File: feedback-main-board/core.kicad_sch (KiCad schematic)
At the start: 38 parts, among them SW1 SW_SPDT, SW2 SW_SPDT, U1 TL074, U2 TL074

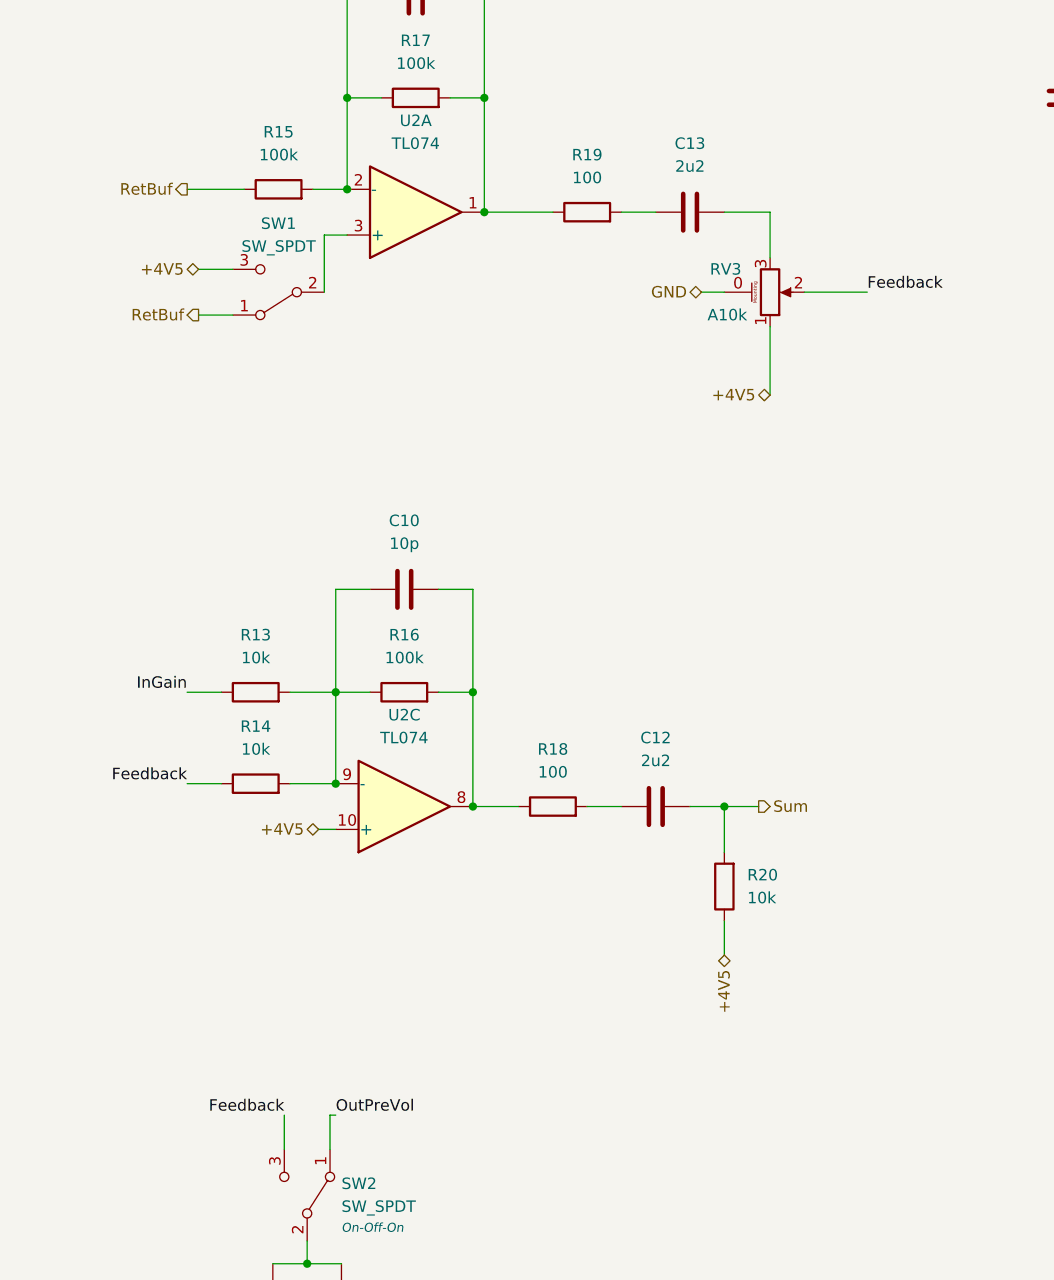
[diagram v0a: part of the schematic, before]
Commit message: Move clipping to pre-feedback
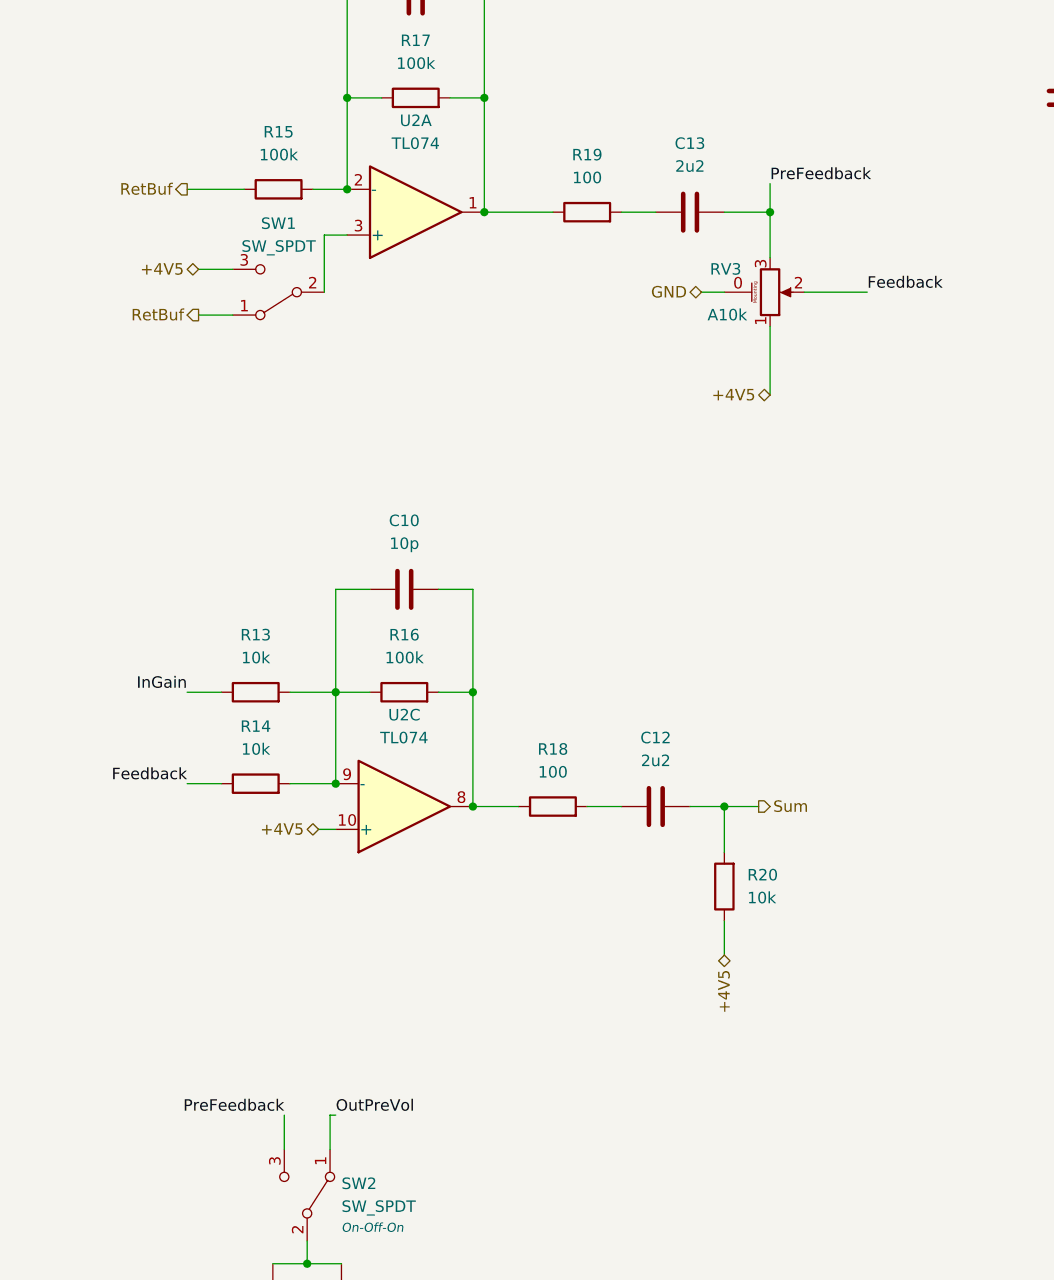
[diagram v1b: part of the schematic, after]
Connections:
- net Feedback: no longer SW2.3 (C)
- net PreFeedback: now reaches C13.2, RV3.3
- net PreFeedback: now also SW2.3 (C)
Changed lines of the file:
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@@
   (junction (at 253.365 45.72) (diameter 0) (color 0 0 0 0)
   )
+  (junction (at 207.01 48.26) (diameter 0) (color 0 0 0 0)
+  )
   (junction (at 93.98 171.45) (diameter 0) (color 0 0 0 0)
   )
@@
   )
   (wire (pts (xy 170.18 101.6) (xy 173.99 101.6))
+    (stroke (width 0) (type default) (color 0 0 0 0))
+  )
+  (wire (pts (xy 207.01 45.085) (xy 207.01 48.26))
     (stroke (width 0) (type default) (color 0 0 0 0))
   )
@@
     (effects (font (size 1 1) italic) (justify left bottom))
   )
-  (label "Feedback" (at 153.035 148.59 180)
+  (label "PreFeedback" (at 153.035 148.59 180)
     (effects (font (size 1.27 1.27)) (justify right bottom))
   )
@@
     (effects (font (size 1.27 1.27)) (justify left bottom))
   )
+  (label "PreFeedback" (at 207.01 45.085 0)
+    (effects (font (size 1.27 1.27)) (justify left bottom))
+  )

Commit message: Changes pre-rev3
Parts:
- C10, C11: LCSC (none) -> C1634
- C12, C13, C5, C6, C7, C8, C9, D2, D3, D4, D5, RV1, RV2, RV3, SW1, SW2: LCSC (none) -> DNP
- C14, C15: LCSC (none) -> C14663; Mouser (none) -> 581-06035C105MAT2A
- R10, R11, R18, R19, R9: LCSC (none) -> C22775
- R12, R13, R14, R20: LCSC (none) -> C25804
- R15, R16, R17, R6, R8: LCSC (none) -> C25803
- R5, R7: LCSC (none) -> C22935
- U1, U2: LCSC (none) -> C6964
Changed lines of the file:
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@@
   (title_block
     (title "Read/Repeat")
-    (date "2025-01-24")
-    (rev "v1rev1")
+    (date "2025-03-14")
+    (rev "v1rev3")
     (company "Pedal Markt / Andrei Salomatin")
   )
@@
     )
     (property "Mouser" "595-TL074IDR" (id 4) (at 167.64 48.26 0)
+      (effects (font (size 1.27 1.27)) hide)
+    )
+    (property "LCSC" "C6964" (id 5) (at 167.64 48.26 0)
       (effects (font (size 1.27 1.27)) hide)
     )
@@
       (effects (font (size 1.27 1.27)) hide)
     )
+    (property "LCSC" "DNP" (id 5) (at 35.56 116.84 0)
+      (effects (font (size 1.27 1.27)) hide)
+    )
     (pin "1")
     (pin "2")
@@
     )
     (property "Datasheet" "~" (id 3) (at 167.64 24.13 0)
+      (effects (font (size 1.27 1.27)) hide)
+    )
+    (property "LCSC" "C1634" (id 4) (at 167.64 24.13 0)
       (effects (font (size 1.27 1.27)) hide)
     )
@@
       (effects (font (size 1.27 1.27)) hide)
     )
+    (property "LCSC" "DNP" (id 4) (at 207.01 57.15 0)
+      (effects (font (size 1.27 1.27)) hide)
+    )
     (pin "0")
     (pin "1")
@@
       (effects (font (size 1.27 1.27)) hide)
     )
+    (property "LCSC" "C22775" (id 4) (at 73.66 48.26 0)
+      (effects (font (size 1.27 1.27)) hide)
+    )
     (pin "1")
     (pin "2")
@@
       (effects (font (size 1.27 1.27)) hide)
     )
+    (property "LCSC" "DNP" (id 4) (at 35.56 50.8 0)
+      (effects (font (size 1.27 1.27)) hide)
+    )
     (pin "1")
     (pin "2")
@@
       (effects (font (size 1.27 1.27)) hide)
     )
+    (property "LCSC" "C25803" (id 4) (at 152.4 45.72 0)
+      (effects (font (size 1.27 1.27)) hide)
+    )
     (pin "1")
     (pin "2")
@@
       (effects (font (size 1.27 1.27)) hide)
     )
+    (property "LCSC" "DNP" (id 5) (at 85.09 171.45 0)
+      (effects (font (size 1.27 1.27)) hide)
+    )
     (pin "1")
     (pin "2")
@@
     )
     (property "Datasheet" "~" (id 3) (at 151.765 179.07 0)
+      (effects (font (size 1.27 1.27)) hide)
+    )
+    (property "LCSC" "DNP" (id 4) (at 151.765 179.07 0)
       (effects (font (size 1.27 1.27)) hide)
     )
@@
       (effects (font (size 1.27 1.27)) hide)
     )
+    (property "LCSC" "DNP" (id 5) (at 85.09 114.3 0)
+      (effects (font (size 1.27 1.27)) hide)
+    )
     (pin "1")
     (pin "2")
@@
       (effects (font (size 1.27 1.27)) hide)
     )
+    (property "LCSC" "C22775" (id 4) (at 186.69 48.26 0)
+      (effects (font (size 1.27 1.27)) hide)
+    )
     (pin "1")
     (pin "2")
@@
       (effects (font (size 1.27 1.27)) hide)
     )
+    (property "LCSC" "C25804" (id 5) (at 93.98 123.19 0)
+      (effects (font (size 1.27 1.27)) hide)
+    )
     (pin "1")
     (pin "2")
@@
       (effects (font (size 1.27 1.27)) hide)
     )
+    (property "LCSC" "C25803" (id 4) (at 44.45 124.46 0)
+      (effects (font (size 1.27 1.27)) hide)
+    )
     (pin "1")
     (pin "2")
@@
       (effects (font (size 1.27 1.27)) hide)
     )
+    (property "LCSC" "DNP" (id 4) (at 155.575 157.48 0)
+      (effects (font (size 1.27 1.27)) hide)
+    )
     (pin "1")
     (pin "2")
@@
     )
     (property "Mouser" "595-TL074IDR" (id 4) (at 278.13 35.56 0)
+      (effects (font (size 1.27 1.27)) hide)
+    )
+    (property "LCSC" "C6964" (id 5) (at 278.13 35.56 0)
       (effects (font (size 1.27 1.27)) hide)
     )
@@
       (effects (font (size 1.27 1.27)) hide)
     )
+    (property "Mouser" "581-06035C105MAT2A" (id 4) (at 240.03 35.56 0)
+      (effects (font (size 1.27 1.27)) hide)
+    )
+    (property "LCSC" "C14663" (id 5) (at 240.03 35.56 0)
+      (effects (font (size 1.27 1.27)) hide)
+    )
     (pin "1")
     (pin "2")
@@
       (effects (font (size 1.27 1.27)) hide)
     )
+    (property "LCSC" "DNP" (id 5) (at 194.31 114.3 0)
+      (effects (font (size 1.27 1.27)) hide)
+    )
     (pin "1")
     (pin "2")
@@
       (effects (font (size 1.27 1.27)) hide)
     )
+    (property "LCSC" "DNP" (id 5) (at 85.09 48.26 0)
+      (effects (font (size 1.27 1.27)) hide)
+    )
     (pin "1")
     (pin "2")
@@
       (effects (font (size 1.27 1.27)) hide)
     )
+    (property "LCSC" "C22935" (id 4) (at 25.4 58.42 0)
+      (effects (font (size 1.27 1.27)) hide)
+    )
     (pin "1")
     (pin "2")
@@
       (effects (font (size 1.27 1.27)) hide)
     )
+    (property "LCSC" "C25803" (id 4) (at 25.4 124.46 0)
+      (effects (font (size 1.27 1.27)) hide)
+    )
     (pin "1")
     (pin "2")
@@
     )
     (property "Mouser" "595-TL074IDR" (id 4) (at 255.905 35.56 0)
+      (effects (font (size 1.27 1.27)) hide)
+    )
+    (property "LCSC" "C6964" (id 5) (at 255.905 35.56 0)
       (effects (font (size 1.27 1.27)) hide)
     )
@@
       (effects (font (size 1.27 1.27)) hide)
     )
+    (property "LCSC" "C22775" (id 4) (at 73.66 114.3 0)
+      (effects (font (size 1.27 1.27)) hide)
+    )
     (pin "1")
     (pin "2")
@@
       (effects (font (size 1.27 1.27)) hide)
     )
+    (property "LCSC" "DNP" (id 4) (at 93.98 62.23 0)
+      (effects (font (size 1.27 1.27)) hide)
+    )
     (pin "0")
     (pin "1")
@@
       (effects (font (size 1.27 1.27)) hide)
     )
+    (property "LCSC" "C22775" (id 4) (at 182.88 114.3 0)
+      (effects (font (size 1.27 1.27)) hide)
+    )
     (pin "1")
     (pin "2")
@@
     )
     (property "Datasheet" "~" (id 3) (at 159.385 168.91 0)
+      (effects (font (size 1.27 1.27)) hide)
+    )
+    (property "LCSC" "DNP" (id 4) (at 159.385 168.91 0)
       (effects (font (size 1.27 1.27)) hide)
     )
@@
       (effects (font (size 1.27 1.27)) hide)
     )
+    (property "LCSC" "DNP" (id 4) (at 114.3 177.165 0)
+      (effects (font (size 1.27 1.27)) hide)
+    )
     (pin "0")
     (pin "1")
@@
     )
     (property "Datasheet" "~" (id 3) (at 264.16 35.56 0)
+      (effects (font (size 1.27 1.27)) hide)
+    )
+    (property "Mouser" "581-06035C105MAT2A" (id 4) (at 264.16 35.56 0)
+      (effects (font (size 1.27 1.27)) hide)
+    )
+    (property "LCSC" "C14663" (id 5) (at 264.16 35.56 0)
       (effects (font (size 1.27 1.27)) hide)
     )
@@
     )
     (property "Mouser" "595-TL074IDR" (id 4) (at 57.15 171.45 0)
+      (effects (font (size 1.27 1.27)) hide)
+    )
+    (property "LCSC" "C6964" (id 5) (at 57.15 171.45 0)
       (effects (font (size 1.27 1.27)) hide)
     )
@@
       (effects (font (size 1.27 1.27)) hide)
     )
+    (property "LCSC" "DNP" (id 4) (at 152.4 57.15 0)
+      (effects (font (size 1.27 1.27)) hide)
+    )
     (pin "1")
     (pin "2")
@@
       (effects (font (size 1.27 1.27)) hide)
     )
+    (property "LCSC" "C22775" (id 4) (at 73.66 171.45 0)
+      (effects (font (size 1.27 1.27)) hide)
+    )
     (pin "1")
     (pin "2")
@@
       (effects (font (size 1.27 1.27)) hide)
     )
+    (property "LCSC" "C25804" (id 4) (at 149.86 111.76 0)
+      (effects (font (size 1.27 1.27)) hide)
+    )
     (pin "1")
     (pin "2")
@@
       (effects (font (size 1.27 1.27)) hide)
     )
+    (property "LCSC" "C25804" (id 4) (at 149.86 101.6 0)
+      (effects (font (size 1.27 1.27)) hide)
+    )
     (pin "1")
     (pin "2")
@@
       (effects (font (size 1.27 1.27)) hide)
     )
+    (property "LCSC" "C1634" (id 4) (at 166.37 90.17 0)
+      (effects (font (size 1.27 1.27)) hide)
+    )
     (pin "1")
     (pin "2")
@@
     )
     (property "Mouser" "595-TL074IDR" (id 4) (at 57.15 114.3 0)
+      (effects (font (size 1.27 1.27)) hide)
+    )
+    (property "LCSC" "C6964" (id 5) (at 57.15 114.3 0)
       (effects (font (size 1.27 1.27)) hide)
     )
@@
       (effects (font (size 1.27 1.27)) hide)
     )
+    (property "LCSC" "C25804" (id 5) (at 201.93 123.19 0)
+      (effects (font (size 1.27 1.27)) hide)
+    )
     (pin "1")
     (pin "2")
@@
     )
     (property "Datasheet" "~" (id 3) (at 44.45 58.42 0)
+      (effects (font (size 1.27 1.27)) hide)
+    )
+    (property "LCSC" "C22935" (id 4) (at 44.45 58.42 0)
       (effects (font (size 1.27 1.27)) hide)
     )
@@
     )
     (property "Mouser" "595-TL074IDR" (id 4) (at 58.42 48.26 0)
+      (effects (font (size 1.27 1.27)) hide)
+    )
+    (property "LCSC" "C6964" (id 5) (at 58.42 48.26 0)
       (effects (font (size 1.27 1.27)) hide)
     )
@@
       (effects (font (size 1.27 1.27)) hide)
     )
+    (property "LCSC" "C25803" (id 4) (at 166.37 101.6 0)
+      (effects (font (size 1.27 1.27)) hide)
+    )
     (pin "1")
     (pin "2")
@@
     )
     (property "Mouser" "595-TL074IDR" (id 4) (at 166.37 114.3 0)
+      (effects (font (size 1.27 1.27)) hide)
+    )
+    (property "LCSC" "C6964" (id 5) (at 166.37 114.3 0)
       (effects (font (size 1.27 1.27)) hide)
     )
@@
       (effects (font (size 1.27 1.27)) hide)
     )
+    (property "LCSC" "C25803" (id 4) (at 167.64 35.56 0)
+      (effects (font (size 1.27 1.27)) hide)
+    )
     (pin "1")
     (pin "2")
@@
       (effects (font (size 1.27 1.27)) hide)
     )
+    (property "LCSC" "DNP" (id 4) (at 159.385 179.07 0)
+      (effects (font (size 1.27 1.27)) hide)
+    )
     (pin "1")
     (pin "2")
@@
     )
     (property "Datasheet" "~" (id 3) (at 151.765 168.91 0)
+      (effects (font (size 1.27 1.27)) hide)
+    )
+    (property "LCSC" "DNP" (id 4) (at 151.765 168.91 0)
       (effects (font (size 1.27 1.27)) hide)
     )
@@
       (effects (font (size 1.27 1.27)) hide)
     )
+    (property "LCSC" "DNP" (id 5) (at 198.12 48.26 0)
+      (effects (font (size 1.27 1.27)) hide)
+    )
